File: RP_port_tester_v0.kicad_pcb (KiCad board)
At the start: 2 copper layers, 82 parts, among them J1 USB_B PORT0, J2 USB_B PORT1, J3 USB_B PORT2, J4 USB_B PORT3, J5 DE9_Pins, J6 DE9_Pins, J7 DE9_Pins, J8 DE9_Pins, J9 UART, Q1 IRLZ44N, SW1 BOOTSEL, U1 AMS1117-3.3, U2 STMPS2151, U3 STMPS2151, U4 FSUSB74MPX, U5 W25Q128JVS, U6 STMPS2151, U7 RP2040, U8 LM2904, Y1 ABM8-272-T3

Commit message: Layout and Tracing
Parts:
- removed the J1 at (81.4, 29.3)
- removed the J2 at (81.4, 44.4)
- removed the J3 at (81.4, 59.4)
- removed the J4 at (81.4, 74.5)
- removed the R6 at (99.3, 33.0)
- removed the R7 at (99.3, 35.5)
- removed the U2 at (151.2, 59.7)
- removed the U3 at (151.2, 64.5)
- added C23: 100n, Capacitor_SMD:C_0603_1608Metric_Pad1.08x0.95mm_HandSolder, F.Cu at (154.5, 98.5)
- added D3: P6SMB6.8, Diode_SMD:D_SMB, F.Cu at (198.5, 44.4)
- added D4: P6SMB6.8, Diode_SMD:D_SMB, F.Cu at (198.5, 69.9)
- added D5: P6SMB6.8, Diode_SMD:D_SMB, F.Cu at (198.5, 94.5)
- added D6: P6SMB6.8, Diode_SMD:D_SMB, F.Cu at (198.5, 119.5)
- added FID1: Fiducial, Fiducial:Fiducial_1mm_Mask2mm, F.Cu at (74.0, 139.0)
- added FID2: Fiducial, Fiducial:Fiducial_1mm_Mask2mm, F.Cu at (82.0, 30.0)
- added FID3: Fiducial, Fiducial:Fiducial_1mm_Mask2mm, F.Cu at (215.0, 37.0)
- added FID4: Fiducial, Fiducial:Fiducial_1mm_Mask2mm, F.Cu at (215.0, 133.0)
- added FID5: Fiducial, Fiducial:Fiducial_1mm_Mask2mm, F.Cu at (135.0, 105.0)
- added H1: TOOLING_HOLE, MountingHole:ToolingHole_1.152mm, F.Cu at (209.0, 27.0)
- added H2: MountingHole, MountingHole:MountingHole_3.2mm_M3, F.Cu at (75.0, 30.0)
- added H3: TOOLING_HOLE, MountingHole:ToolingHole_1.152mm, F.Cu at (72.0, 37.0)
- added H4: MountingHole, MountingHole:MountingHole_3.2mm_M3, F.Cu at (215.0, 30.0)
- added H5: TOOLING_HOLE, MountingHole:ToolingHole_1.152mm, F.Cu at (72.0, 133.0)
- added H6: MountingHole, MountingHole:MountingHole_3.2mm_M3, F.Cu at (215.0, 140.0)
- added J6: USB_B PORT0, My_Library:USB_B_Vertical, F.Cu at (186.0, 43.4)
- added J7: USB_B PORT1, My_Library:USB_B_Vertical, F.Cu at (186.0, 68.4)
- added J8: USB_B PORT2, My_Library:USB_B_Vertical, F.Cu at (186.0, 93.5)
- added J9: USB_B PORT3, My_Library:USB_B_Vertical, F.Cu at (186.0, 118.5)
- added R14: 100k, Resistor_SMD:R_0603_1608Metric_Pad0.98x0.95mm_HandSolder, F.Cu at (107.5, 69.6)
- added R15: 1k, Resistor_SMD:R_0603_1608Metric_Pad0.98x0.95mm_HandSolder, F.Cu at (92.0, 68.6)
- added TP1: TestPoint, TestPoint:TestPoint_Plated_Hole_D2.0mm, F.Cu at (178.0, 39.0)
- added TP2: TestPoint, TestPoint:TestPoint_Plated_Hole_D2.0mm, F.Cu at (160.0, 66.0)
- added TP3: TestPoint, TestPoint:TestPoint_Plated_Hole_D2.0mm, F.Cu at (163.0, 48.0)
- added TP4: TestPoint, TestPoint:TestPoint_Plated_Hole_D2.0mm, F.Cu at (87.0, 95.0)
- added U10: USBLC6-2SC6, Package_TO_SOT_SMD:SOT-23-6, F.Cu at (178.4, 74.9)
- added U11: USBLC6-2SC6, Package_TO_SOT_SMD:SOT-23-6, F.Cu at (178.9, 89.5)
- added U12: USBLC6-2SC6, Package_TO_SOT_SMD:SOT-23-6, F.Cu at (178.9, 114.0)
- added U7: STMPS2151, Package_TO_SOT_SMD:SOT-23-5_HandSoldering, F.Cu at (136.7, 38.5)
- added U8: STMPS2151, Package_TO_SOT_SMD:SOT-23-5_HandSoldering, F.Cu at (136.7, 32.5)
- added U9: USBLC6-2SC6, Package_TO_SOT_SMD:SOT-23-6, F.Cu at (178.4, 50.9)
- Q1: footprint Package_TO_SOT_THT:TO-220-3_Vertical -> Package_TO_SOT_THT:TO-220-3_Horizontal_TabDown
- R10: value 220R -> 1k
- R11: value 390R -> 12k
- R12: value 220R -> 100R
- R13: value 390R -> 1k
- R16: value 70k -> 1k
- R17: value 100k -> 47R
- R18: value 1k -> 120k
- R19: value 12k -> 0R51; footprint Resistor_SMD:R_0603_1608Metric_Pad0.98x0.95mm_HandSolder -> Resistor_THT:R_Axial_DIN0309_L9.0mm_D3.2mm_P15.24mm_Horizontal
- R20: value 100R -> 10k
- R21: value 1k -> 100R
- R22: value 100k -> 220R
- R23: value 1k -> 390R
- R24: value 1k -> 220R
- R25: value 47R -> 390R
- R26: value 120k -> 220R
- R27: value 0R51 -> 390R; footprint Resistor_THT:R_Axial_DIN0309_L9.0mm_D3.2mm_P15.24mm_Horizontal -> Resistor_SMD:R_0603_1608Metric_Pad0.98x0.95mm_HandSolder
- R28: value 10k -> 220R
- R29: value 100R -> 390R
- R8: value 220R -> 70k
- R9: value 390R -> 100k
- moved J4 139.0 mm to (183.9, 132.6)
- moved D8 132.8 mm to (192.5, 33.4)
- moved D7 123.2 mm to (184.5, 33.4)
- moved D10 118.1 mm to (192.5, 58.4)
- moved J3 117.6 mm to (151.4, 132.6)
- moved J1 111.4 mm to (86.4, 132.6)
- moved D9 108.9 mm to (184.5, 58.4)
- moved D12 107.5 mm to (192.5, 83.5)
- moved J2 107.3 mm to (118.9, 132.6)
- moved R27 105.7 mm to (190.0, 83.5), turned to 90 degrees
- moved R29 104.9 mm to (190.0, 108.5), turned to 90 degrees
- moved D14 102.4 mm to (192.5, 108.5)
- moved R28 100.4 mm to (182.0, 108.5), turned to 90 degrees
- moved D11 99.2 mm to (184.5, 83.5)
- moved D13 95.6 mm to (184.5, 108.5)
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- renumbered D6 to D10, D7 to D11, D8 to D12, D9 to D13, D10 to D14, D3 to D7, D4 to D8, D5 to D9, J5 to J1, J6 to J2, J7 to J3, J8 to J4, J9 to J5, R14 to R4, R4 to R5, R5 to R6, R15 to R7, U5 to U2, U4 to U3, U7 to U4, U8 to U5
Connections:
- net /PICO_PORT0_TESTED renamed PICO_PORT0_TESTED
- net /PICO_PORT1_TESTED renamed PICO_PORT1_TESTED
- net /PICO_PORT2_TESTED renamed PICO_PORT2_TESTED
- net /PICO_PORT3_TESTED renamed PICO_PORT3_TESTED
- net /USB3_VBUS_EN renamed USB1_VBUS_EN
- net Net-(C16-Pad2) renamed /Crystal_Out
- net Net-(R2-Pad2) renamed /BOOTSEL_BTN
- net Net-(U7-XIN) renamed /PICO_XIN
- net Net-(U7-XOUT) renamed /PICO_XOUT
- C18 pad 1: Net-(C18-Pad1) -> /PWM_Filt
- C19 pad 1: Net-(U8A-+) -> /Amp Current+
- C20 pad 1: Net-(C20-Pad1) -> /Amp Current Out
- C20 pad 2: Net-(U8A--) -> /Amp Current-
- C21 pad 1: Net-(U8B-+) -> /Amp Gain+
- D10 pad 1: Net-(D6-K) -> Net-(D10-K)
- D11 pad 1: Net-(D7-K) -> Net-(D11-K)
- D11 pad 2: /USB2_VBUS -> /USB Connectors/USB2_VBUS
- D12 pad 1: Net-(D8-K) -> Net-(D12-K)
- D13 pad 1: Net-(D9-K) -> Net-(D13-K)
- D13 pad 2: /USB3_VBUS -> /USB Connectors/USB3_VBUS
- D14 pad 1: Net-(D10-K) -> Net-(D14-K)
- D7 pad 1: Net-(D3-K) -> Net-(D7-K)
- D8 pad 1: Net-(D4-K) -> Net-(D8-K)
- D9 pad 1: Net-(D5-K) -> Net-(D9-K)
- D9 pad 2: /USB1_VBUS -> /USB Connectors/USB1_VBUS
- Q1 pad 1: Net-(Q1-G) -> /FET-Gate
- Q1 pad 3: Net-(Q1-S) -> /Shunt High
- R10 pad 1: Net-(D7-K) -> /PICO_LOAD_PWM
- R10 pad 2: GND -> /PWM_Filt
- R11 pad 1: Net-(D8-K) -> /PWM_Filt
- R11 pad 2: GND -> /Amp Current+
- R12 pad 1: Net-(D9-K) -> /Amp Current Out
- R12 pad 2: GND -> /FET-Gate
- R13 pad 1: Net-(D10-K) -> /Amp Current+
- R16 pad 1: VBUS_TEST -> /Amp Gain Out
- R16 pad 2: /PICO_VBUS_ADC -> /PICO_CURRENT_ADC
- R17 pad 1: /PICO_VBUS_ADC -> /Amp Current-
- R17 pad 2: GND -> /Shunt High
- R18 pad 1: /PICO_LOAD_PWM -> /Amp Gain-
- R18 pad 2: Net-(C18-Pad1) -> /Amp Gain Out
- R19 pad 1: Net-(C18-Pad1) -> /Shunt High
- R19 pad 2: Net-(U8A-+) -> GND
- R20 pad 1: Net-(C20-Pad1) -> /Amp Gain-
- R20 pad 2: Net-(Q1-G) -> GND
- R21 pad 1: Net-(U8A-+) -> /PICO_AUDIO_EN
- R21 pad 2: GND -> Net-(LS1-Pad1)
- R22 pad 1: GND -> Net-(D7-K)
- R22 pad 2: Net-(Q1-G) -> GND
- R23 pad 1: Net-(Q1-S) -> Net-(D8-K)
- R23 pad 2: Net-(U8B-+) -> GND
- R24 pad 1: Net-(R24-Pad1) -> Net-(D9-K)
- R24 pad 2: /PICO_CURRENT_ADC -> GND
- R25 pad 1: Net-(U8A--) -> Net-(D10-K)
- R25 pad 2: Net-(Q1-S) -> GND
- R26 pad 1: Net-(U8B--) -> Net-(D11-K)
- R26 pad 2: Net-(R24-Pad1) -> GND
- R27 pad 1: Net-(Q1-S) -> Net-(D12-K)
- R28 pad 1: Net-(U8B--) -> Net-(D13-K)
- R29 pad 1: /PICO_AUDIO_EN -> Net-(D14-K)
- R29 pad 2: Net-(LS1-Pad1) -> GND
- R3 pad 1: /PICO_USB_D- -> /PICO_USB_D+
- R4 pad 1: /PICO_USB_D+ -> /PICO_USB_D-
- R8 pad 1: Net-(D5-K) -> VBUS_TEST
- R8 pad 2: GND -> /PICO_VBUS_ADC
- R9 pad 1: Net-(D6-K) -> /PICO_VBUS_ADC
- U3 pad 10: /USB2_D+ -> USB2_D+
- U3 pad 11: /USB1_D+ -> USB1_D+
- U3 pad 12: /USB1_D- -> USB1_D-
- U3 pad 13: /USB0_D+ -> USB0_D+
- U3 pad 14: /USB0_D- -> USB0_D-
- U3 pad 7: /USB3_D- -> USB3_D-
- U3 pad 8: /USB3_D+ -> USB3_D+
- U3 pad 9: /USB2_D- -> USB2_D-
- U4 pad 12: /USB1_VBUS_EN -> USB3_VBUS_EN
- U4 pad 13: /USB2_VBUS_EN -> USB2_VBUS_EN
- U4 pad 35: /PICO_AUDIO_EN -> unconnected-(U4-GPIO23-Pad35)
- U4 pad 5: unconnected-(U7-GPIO3-Pad5) -> /PICO_LOAD_PWM
- U4 pad 7: unconnected-(U7-GPIO5-Pad7) -> /PICO_AUDIO_EN
- U4 pad 8: /PICO_LOAD_PWM -> unconnected-(U4-GPIO6-Pad8)
- U5 pad 1: Net-(C20-Pad1) -> /Amp Current Out
- U5 pad 2: Net-(U8A--) -> /Amp Current-
- U5 pad 3: Net-(U8A-+) -> /Amp Current+
- U5 pad 5: Net-(U8B-+) -> /Amp Gain+
- U5 pad 6: Net-(U8B--) -> /Amp Gain-
- U5 pad 7: Net-(R24-Pad1) -> /Amp Gain Out
- U6 pad 5: /USB3_VBUS -> /USB Connectors/USB1_VBUS
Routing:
- net /USB Connectors/USB3_VBUS: track 0.00 -> 193.8 mm, vias 0 -> 2
- net VBUS: track 0.00 -> 186.9 mm, vias 0 -> 2
- net /USB Connectors/USB2_VBUS: track 0.00 -> 168.3 mm, vias 0 -> 2
- net PICO_PORT0_TESTED: track 0.00 -> 161.8 mm
- net /USB Connectors/USB1_VBUS: track 0.00 -> 140.2 mm, vias 0 -> 2
- net PICO_PORT1_TESTED: track 0.00 -> 135.3 mm
- net /PICO_VBUS_ADC: track 0.00 -> 111.8 mm, vias 0 -> 4
- net PICO_PORT2_TESTED: track 0.00 -> 106.4 mm
- net VBUS_TEST: track 0.00 -> 105.3 mm, vias 0 -> 3
- net /Amp Gain Out: track 0.00 -> 103.1 mm, vias 0 -> 2
- net +3.3V: track 0.00 -> 103.0 mm, vias 0 -> 2
- net USB3_VBUS_EN: track 0.00 -> 95.1 mm, vias 0 -> 10
- net USB2_VBUS_EN: track 0.00 -> 89.4 mm, vias 0 -> 8
- net GND: track 0.00 -> 88.5 mm, vias 0 -> 60
- net USB1_VBUS_EN: track 0.00 -> 83.4 mm, vias 0 -> 6
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- added copper zone on F.Cu, net +3.3V
- added copper zone on B.Cu, net GND
- added copper zone on F.Cu, net GND
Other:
- board outline added: 150 x 119 mm

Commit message: Final layout and routing
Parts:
- added G***: LOGO, Graphics:FMTIS, F.Cu at (99.0, 41.7)
- added G***: LOGO, LOGO, F.Cu at (144.0, 78.0)
- C1, C10, C11, C12, C13, C14, C19, C21, C22, C23, C4, C5, C8, C9: value 100n -> 100nF
- C15, C16: value 15p -> 15pF
- C17, C3: value 22u -> 22uF
- C18, C6, C7: value 1u -> 1uF
- C2: value 10u -> 10uF
- C20: value 2n2 -> 2.2nF
- R5: value 180R -> 220R
- R8: value 70k -> 68k
- moved R27 11.3 mm to (179.1, 80.5), turned to 180 degrees
- moved R29 11.3 mm to (179.0, 106.0), turned to 180 degrees
- moved R23 11.3 mm to (179.0, 31.0), turned to 180 degrees
- moved R25 11.2 mm to (179.0, 56.5), turned to 180 degrees
- moved R12 6.50 mm to (112.0, 69.6)
- moved R14 6.50 mm to (114.0, 69.6)
- moved R26 3.00 mm to (179.0, 83.5), turned to 180 degrees
- moved R28 3.00 mm to (179.0, 108.5), turned to 180 degrees
- moved R22 2.99 mm to (179.0, 33.5), turned to 180 degrees
- moved R24 2.99 mm to (179.0, 58.5), turned to 180 degrees
- moved C21 2.83 mm to (84.0, 75.5)
- moved C18 2.50 mm to (106.5, 76.0)
- moved C19 2.50 mm to (101.2, 77.7)
- moved R10 2.50 mm to (108.2, 77.7)
- moved R11 2.50 mm to (104.7, 77.7)
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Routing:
- net +3.3V: track 103.0 -> 124.2 mm
- net Net-(D12-K): track 2.84 -> 13.7 mm
- net Net-(D8-K): track 2.84 -> 13.6 mm
- net Net-(D14-K): track 2.84 -> 13.6 mm
- net Net-(D10-K): track 2.84 -> 13.4 mm
- net +1V1: track 29.1 -> 34.9 mm, vias 2 -> 3
- net /USB Connectors/USB3_VBUS: track 193.8 -> 197.3 mm
- net /FET-Gate: track 14.3 -> 17.5 mm
- net /Amp Current+: track 5.87 -> 8.86 mm
- net /Shunt High: track 10.4 -> 13.1 mm
- net /PICO_LOAD_PWM: track 42.6 -> 40.4 mm, vias 2 -> 0
- net /Amp Gain-: track 4.98 -> 7.08 mm
- net /Amp Current Out: track 24.1 -> 26.2 mm, vias 0 -> 2
- net USB3_D+: track 39.5 -> 41.4 mm
- net /Amp Gain Out: track 103.1 -> 105.0 mm
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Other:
- outline, holes or cut-outs redrawn
- board text added: "3.3V"
- board text added: "FMTIS FÄLT GA BODEN"
- board text added: "GROUND"
- board text added: "USB Testare + Seriel Loopbacks ALBIN NORBÄCK & GÖRAN LARSSON"
- board text added: "V0.1 10/25"
- board text added: "VBUS"
- board text added: "VBUS TEST"
- board text added: "VBUS_UNDER_TEST"

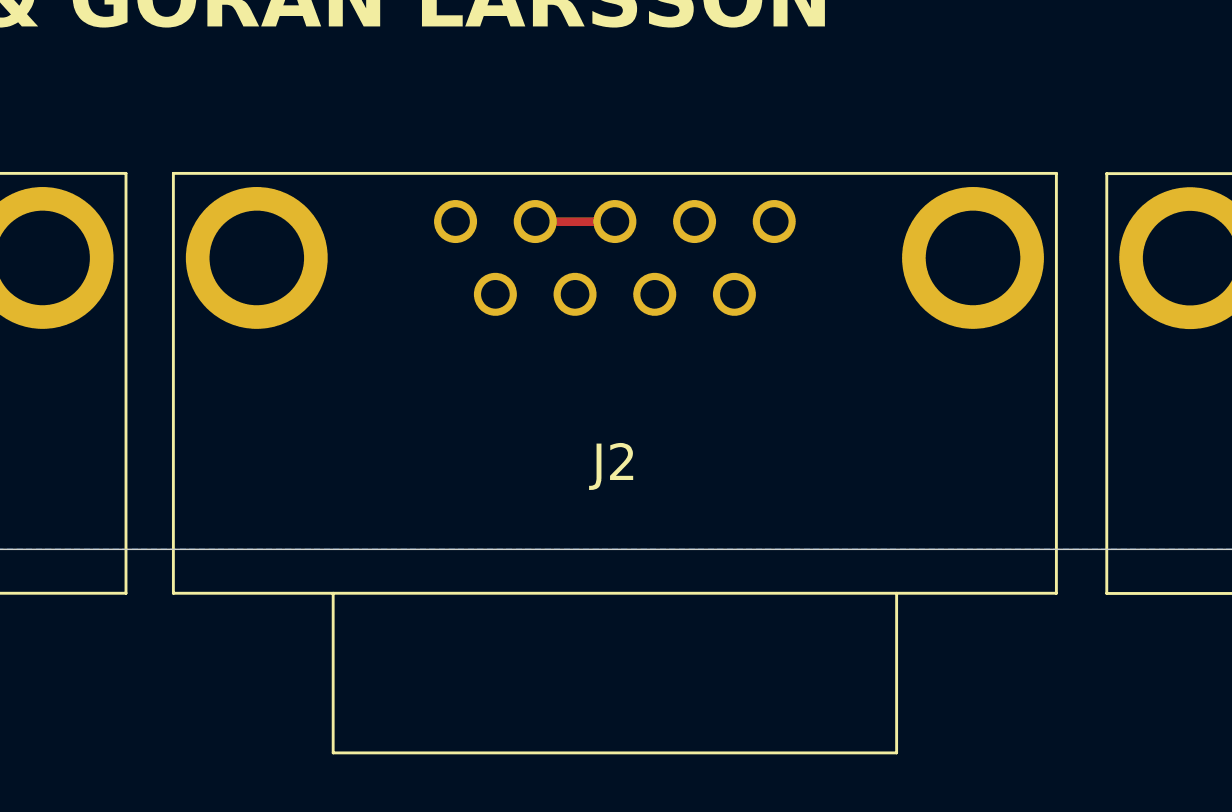
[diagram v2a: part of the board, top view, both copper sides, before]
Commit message: Fix DB9 port misalignment
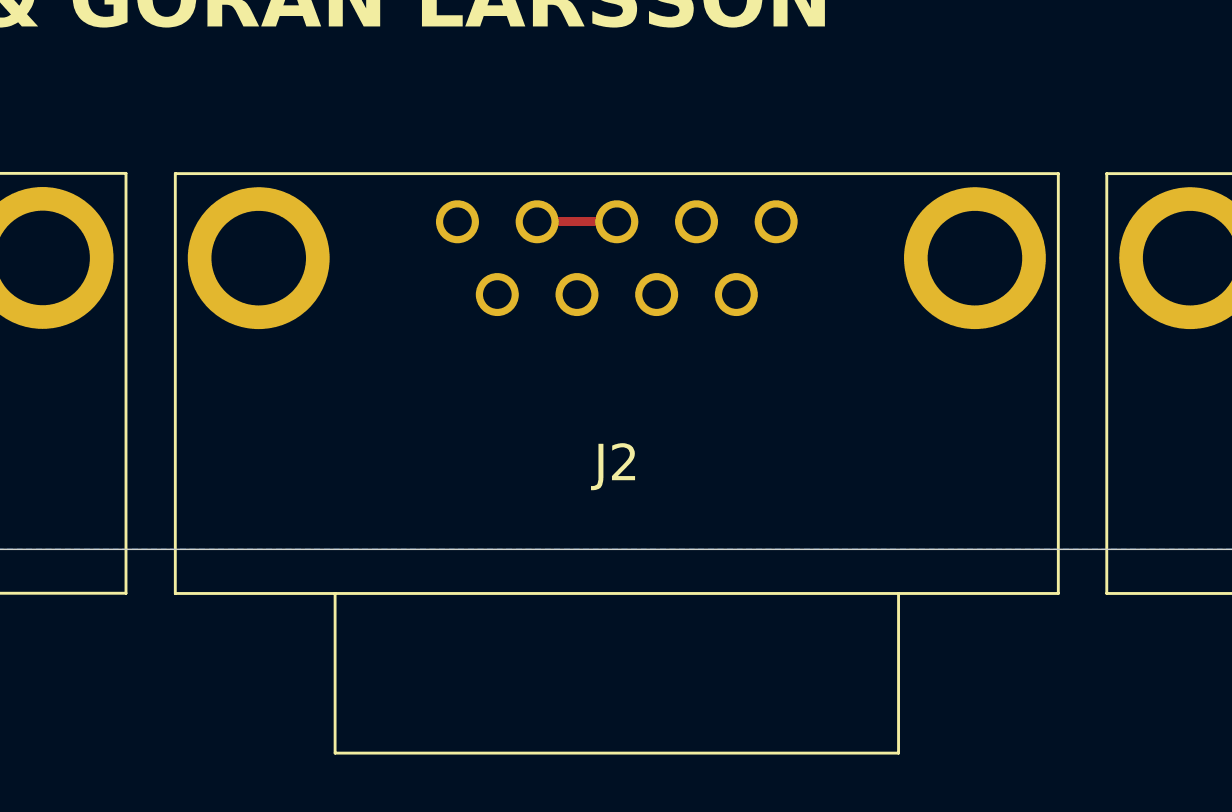
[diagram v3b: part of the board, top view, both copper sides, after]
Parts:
- moved J2 0.07 mm to (118.9, 132.6)
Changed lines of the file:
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@@
 	(footprint "My_Library:DB9_Horizontal"
 		(layer "F.Cu")
-		(at 118.872824 132.562395)
+		(at 118.94 132.57)
 		(descr "2301844-1-2")
 		(tags "Connector")
@@
 			(fill yes)
 			(layer "F.SilkS")
-			(net 103952746)
 		)
 		(embedded_fonts no)
